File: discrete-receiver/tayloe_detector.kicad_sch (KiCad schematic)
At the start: 32 parts, among them U1 SN74CBT3253DBQR, U2 OPA1612AxD, U3 OPA1612AxD

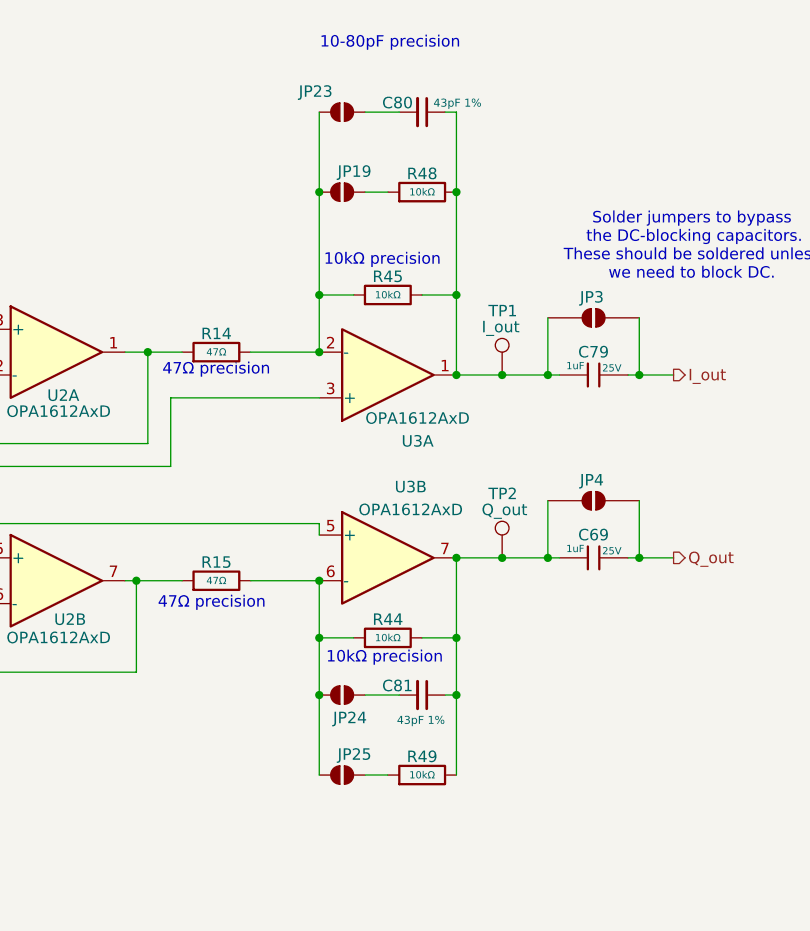
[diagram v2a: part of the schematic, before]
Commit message: Swapped out opamp feedback resistors for 0805
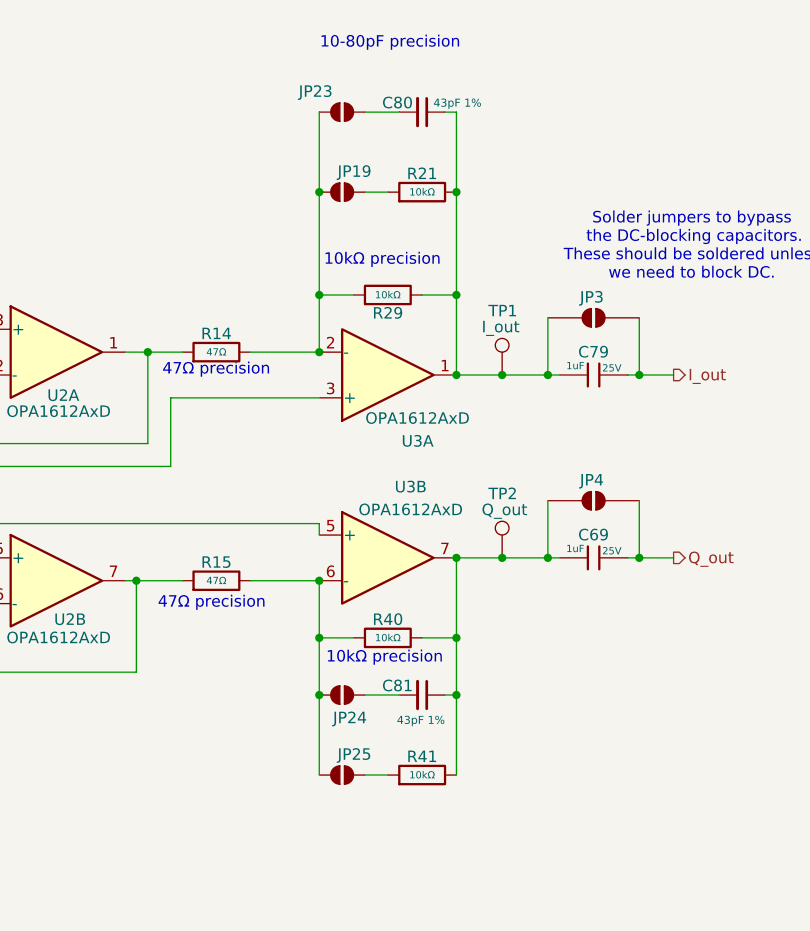
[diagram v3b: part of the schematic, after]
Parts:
- removed R44, R45, R48, R49: 10kΩ, PCM_JLCPCB:R_0402, symbol PCM_JLCPCB-Resistors:0402,10kΩ
- added R21, R29, R40, R41: 10kΩ, PCM_JLCPCB:R_0805, symbol PCM_JLCPCB-Resistors:0805,10kΩ
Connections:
- net at C79.1, C80.1, JP3.2 (B)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: now also R21.2, R29.2
- net at JP25.1 (A): now also R41.1
- net at C69.1, C81.1, JP4.2 (B)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: now also R40.2, R41.2
- net at JP24.2 (B), JP25.2 (B), R15.2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: now also R40.1
- net at JP19.2 (B), JP23.2 (B), R14.2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: now also R29.1
- net at JP19.1 (A): now also R21.1

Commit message: Made ERC progress
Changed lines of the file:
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@@
-		)
-	)
-	(hierarchical_label "LO_VFO"
-		(shape input)
-		(at 8.3708 0.8096 180)
-		(effects
-			(font
-				(size 1.27 1.27)
-			)
-			(justify right)
 		)
 	)

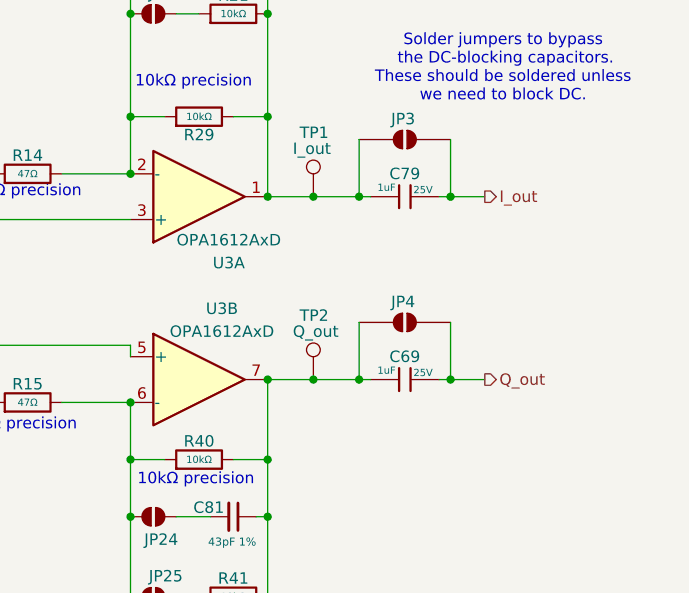
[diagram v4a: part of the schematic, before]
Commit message: Updated 1uF after tayloe to 10uF
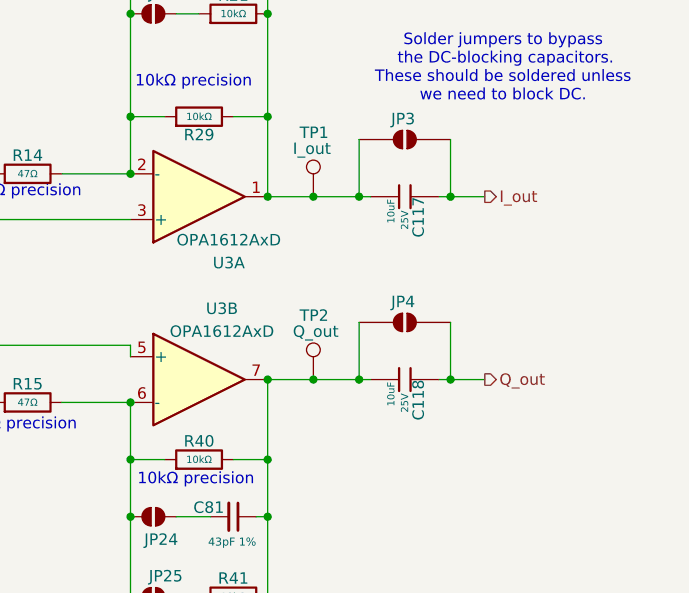
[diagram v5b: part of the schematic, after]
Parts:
- removed C69, C79: 1uF, PCM_JLCPCB:C_0402, symbol PCM_JLCPCB-Capacitors:0402,1uF
- added C117, C118: 10uF, PCM_JLCPCB:C_0603, symbol PCM_JLCPCB-Capacitors:0603,10uF,(2)
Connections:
- net I_out: now also C117.1
- net Q_out: now also C118.1
- net at C80.1, JP3.2 (B), R21.2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: now also C117.2
- net at C81.1, JP4.2 (B), R40.2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: now also C118.2

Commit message: Add components
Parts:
- removed R29, R40: 10kΩ, PCM_JLCPCB:R_0805, symbol PCM_JLCPCB-Resistors:0805,10kΩ
- removed TP1: I_out, TestPoint:TestPoint_Pad_1.5x1.5mm, symbol Connector:TestPoint
- removed TP2: Q_out, TestPoint:TestPoint_Pad_1.5x1.5mm, symbol Connector:TestPoint
- added R29, R40: 1.5kΩ, PCM_JLCPCB:R_0805, symbol PCM_JLCPCB-Resistors:0805,1.5kΩ
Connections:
- net at C117.2, C80.1, JP3.2 (B)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: now also R29.2
- net at JP24.2 (B), JP25.2 (B), R15.2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: now also R40.1
- net at C118.2, C81.1, JP4.2 (B)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: now also R40.2
- net at JP19.2 (B), JP23.2 (B), R14.2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: now also R29.1
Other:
- note removed: "10kΩ precision"

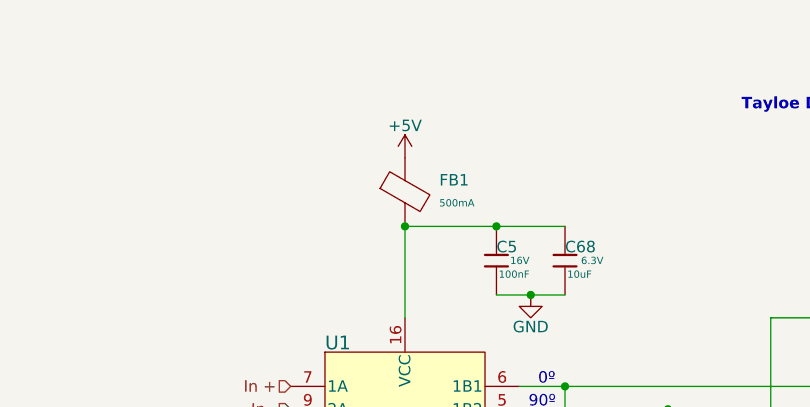
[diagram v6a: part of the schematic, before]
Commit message: shrinked PCB; left digital for peter to finish
The PCB has been shrunk to appropriate size for JLCPCB not adding additional charges. I've left the digital section for Peter to shrink and put in the bound of the board.
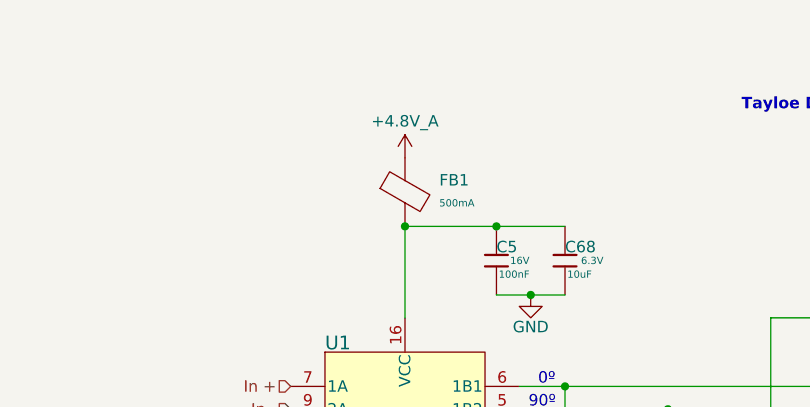
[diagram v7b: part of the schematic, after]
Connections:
- net +5V renamed +4.8V_A
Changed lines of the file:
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@@
+	)
+	(symbol
+		(lib_id "power:+5V")
+		(at 82.55 67.31 0)
+		(unit 1)
+		(body_style 1)
+		(exclude_from_sim no)
+		(in_bom yes)
+		(on_board yes)
+		(in_pos_files yes)
+		(dnp no)
+		(property "Reference" "#PWR0151"
+			(at 82.55 71.12 0)
+			(hide yes)
+			(show_name no)
+			(do_not_autoplace no)
+			(effects
+				(font
+					(size 1.27 1.27)
+				)
+			)
+		)
+		(property "Value" "+4.8V_A"
+			(at 82.55 63.246 0)
+			(show_name no)
+			(do_not_autoplace no)
+			(effects
+				(font
+					(size 1.27 1.27)
+				)
+			)
+		)
+		(property "Footprint" ""
+			(at 82.55 67.31 0)
+			(hide yes)
+			(show_name no)
+			(do_not_autoplace no)
+			(effects
+				(font
+					(size 1.27 1.27)
+				)
+			)
+		)
+		(property "Datasheet" ""
+			(at 82.55 67.31 0)
+			(hide yes)
+			(show_name no)
+			(do_not_autoplace no)
+			(effects
+				(font
+					(size 1.27 1.27)
+				)
+			)
+		)
+		(property "Description" "Power symbol creates a global label with name \"+5V\""
+			(at 82.55 67.31 0)
+			(hide yes)
+			(show_name no)
+			(do_not_autoplace no)
+			(effects
+				(font
+					(size 1.27 1.27)
+				)
+			)
+		)
+		(pin "1"
+		)
+		(instances
+			(project "diode_tayloe_sdr"
+				(path "/d18d178d-3f10-4d68-9036-eae71a7d091a/c96fbd90-62d0-401a-a1f5-d4c4d983c9a4/751ff83c-860e-458a-b47c-a02b34d5585d"
+					(reference "#PWR0151")
+					(unit 1)
+				)
+			)
+		)
 	)
 	(symbol
@@
 					(unit 1)
 				)
-			)
-		)
-	)
-	(symbol
-		(lib_id "power:+5V")
-		(at 82.55 67.31 0)
-		(unit 1)
-		(body_style 1)
-		(exclude_from_sim no)
-		(in_bom yes)
-		(on_board yes)
-		(in_pos_files yes)
-		(dnp no)
-		(property "Reference" "#PWR04"
-			(at 82.55 71.12 0)
-			(hide yes)
-			(show_name no)
-			(do_not_autoplace no)
-			(effects
-				(font
-					(size 1.27 1.27)
-				)
-			)
-		)
-		(property "Value" "+5V"
-			(at 82.55 63.754 0)
-			(show_name no)
-			(do_not_autoplace no)
-			(effects
-				(font
-					(size 1.27 1.27)
-				)
-			)
-		)
-		(property "Footprint" ""
-			(at 82.55 67.31 0)
-			(hide yes)
-			(show_name no)
-			(do_not_autoplace no)
-			(effects
-				(font
-					(size 1.27 1.27)
-				)
-			)
-		)
-		(property "Datasheet" ""
-			(at 82.55 67.31 0)
-			(hide yes)
-			(show_name no)
-			(do_not_autoplace no)
-			(effects
-				(font
-					(size 1.27 1.27)
-				)
-			)
-		)
-		(property "Description" "Power symbol creates a global label with name \"+5V\""
-			(at 82.55 67.31 0)
-			(hide yes)
-			(show_name no)
-			(do_not_autoplace no)
-			(effects
-				(font
-					(size 1.27 1.27)
-				)
-			)
-		)
-		(pin "1"
-		)
-		(instances
-			(project "diode_tayloe_sdr"
-				(path "/d18d178d-3f10-4d68-9036-eae71a7d091a/c96fbd90-62d0-401a-a1f5-d4c4d983c9a4/751ff83c-860e-458a-b47c-a02b34d5585d"
-					(reference "#PWR04")
-					(unit 1)
-				)

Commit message: Updated JLC part numbers because some parts were out of stock
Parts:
- U2, U3: LCSC (none) -> C94590
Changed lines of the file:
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@@
 			)
 		)
+		(property "LCSC" "C94590"
+			(at 156.21 87.63 0)
+			(hide yes)
+			(show_name no)
+			(do_not_autoplace no)
+			(effects
+				(font
+					(size 1.27 1.27)
+				)
+			)
+		)
 		(pin "7"
 		)
@@
 			)
 		)
+		(property "LCSC" "C94590"
+			(at 123.19 165.1 0)
+			(hide yes)
+			(show_name no)
+			(do_not_autoplace no)
+			(effects
+				(font
+					(size 1.27 1.27)
+				)
+			)
+		)
 		(pin "1"
 		)
@@
 			)
 		)
+		(property "LCSC" "C94590"
+			(at 92.71 165.1 0)
+			(hide yes)
+			(show_name no)
+			(do_not_autoplace no)
+			(effects
+				(font
+					(size 1.27 1.27)
+				)
+			)
+		)
 		(pin "7"
 		)
@@
 			)
 		)
+		(property "LCSC" "C94590"
+			(at 156.21 113.03 0)
+			(hide yes)
+			(show_name no)
+			(do_not_autoplace no)
+			(effects
+				(font
+					(size 1.27 1.27)
+				)
+			)
+		)
 		(pin "7"
 		)
@@
 			)
 		)
+		(property "LCSC" "C94590"
+			(at 193.04 110.49 0)
+			(hide yes)
+			(show_name no)
+			(do_not_autoplace no)
+			(effects
+				(font
+					(size 1.27 1.27)
+				)
+			)
+		)
 		(pin "1"
 		)
@@
 			(at 193.04 90.17 0)
 			(hide yes)
+			(show_name no)
+			(do_not_autoplace no)
+			(effects
+				(font
+					(size 1.27 1.27)
+				)
+			)
+		)
+		(property "LCSC" "C94590"
+			(at 193.04 90.17 0)
+			(hide yes)
